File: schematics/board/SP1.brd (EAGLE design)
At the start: 30 x 38 mm, 12 parts

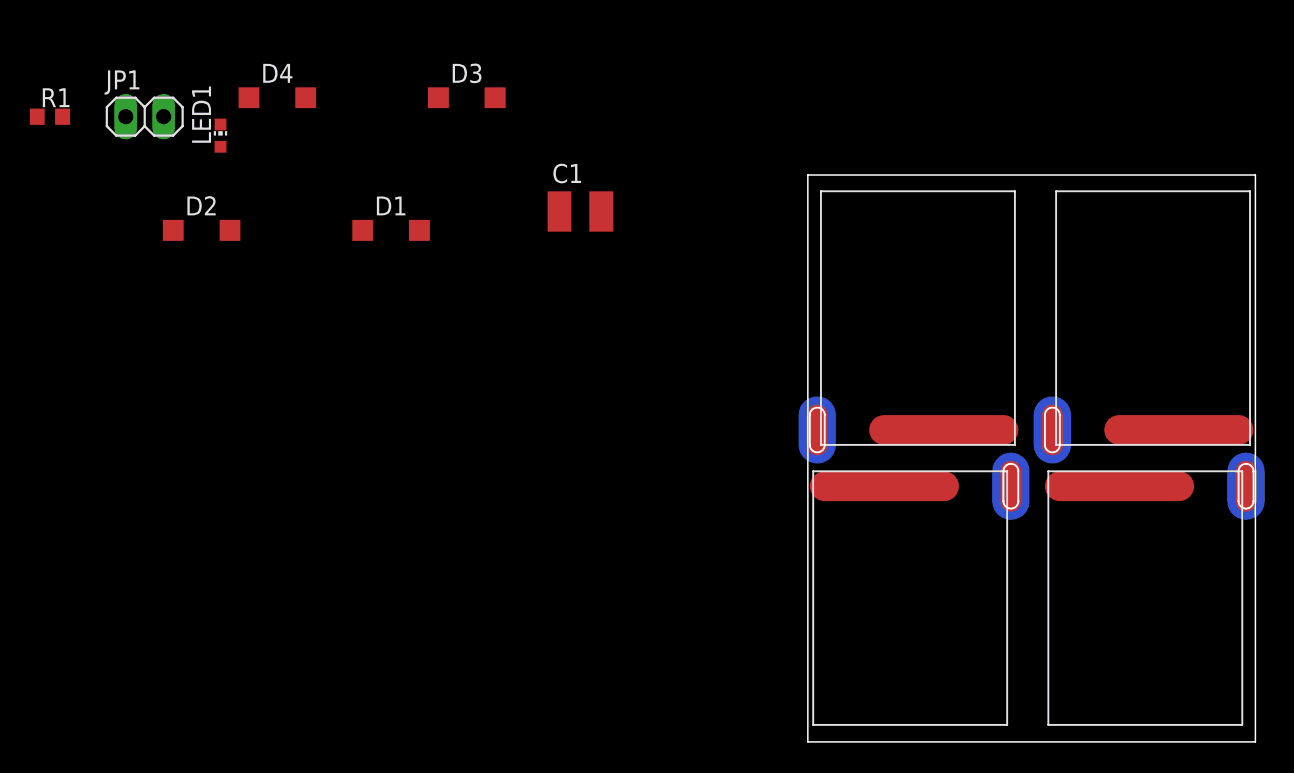
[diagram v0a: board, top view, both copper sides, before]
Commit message: развёл плату солнечных панелей(на деньги)
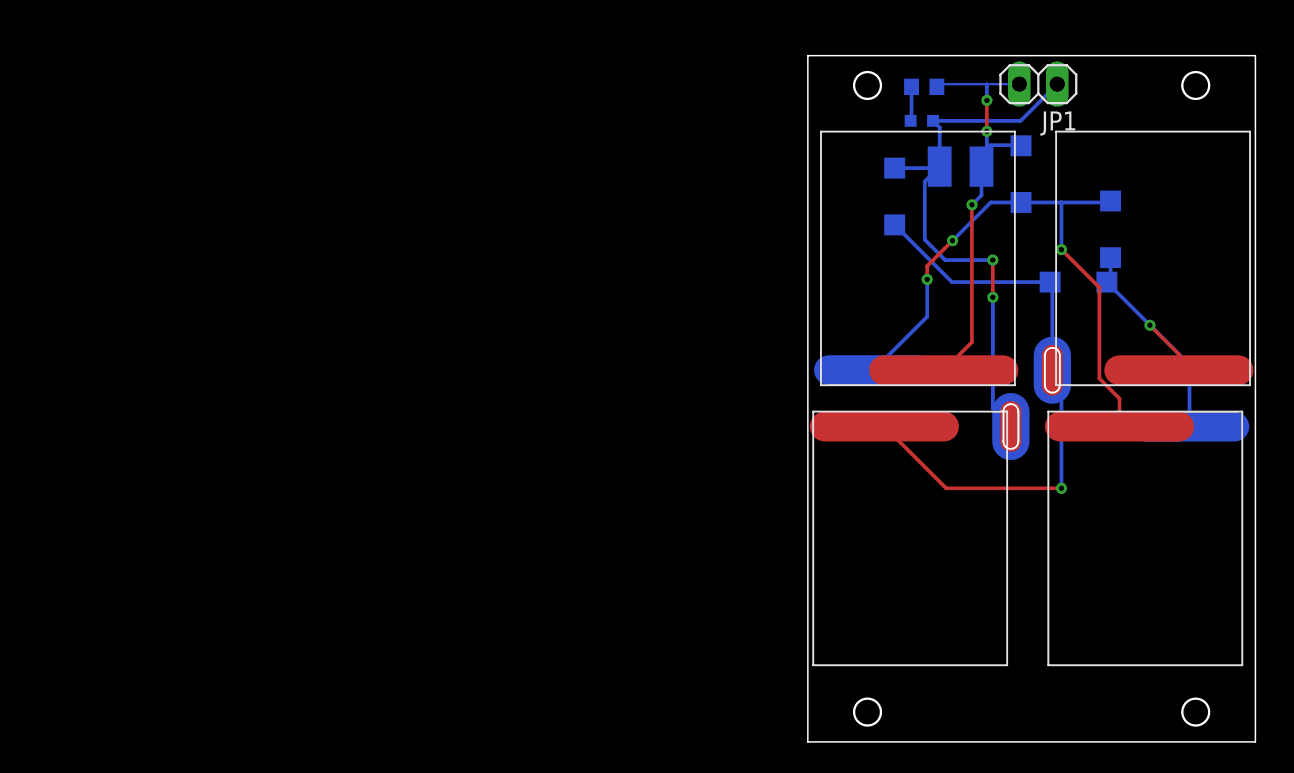
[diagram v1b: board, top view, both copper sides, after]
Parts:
- U$1, U$2: value SOLAR-2_0 -> SOLAR-2_1; device CanCubeSat:SOLAR_0-2 -> CanCubeSat:SOLAR_1-2
- moved D2 60.9 mm to (20.3, 34.4), flipped to the bottom, turned to 90 degrees
- moved JP1 59.9 mm to (15.4, 44.1), turned to 180 degrees
- moved R1 58.6 mm to (7.80, 43.9), flipped to the bottom
- moved LED1 47.0 mm to (7.64, 41.6), flipped to the bottom, turned to 90 degrees
- moved D3 42.8 mm to (18.1, 30.8), flipped to the bottom, turned to 180 degrees
- moved D1 42.4 mm to (14.3, 38.1), flipped to the bottom, turned to 90 degrees
- moved D4 41.9 mm to (5.82, 36.6), flipped to the bottom, turned to 270 degrees
- moved C1 25.7 mm to (10.2, 38.6), flipped to the bottom
- moved U$2 4.00 mm to (22.6, 13.6)
- moved U$4 4.00 mm to (6.86, 13.6)
- moved U$1 4.00 mm to (7.38, 32.4)
- moved U$3 4.00 mm to (23.1, 32.4)
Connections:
- net N$1: now also U$1.OUT; no longer U$1.OUT-2, U$1.OUT-21
- net N$2: now also U$2.OUT; no longer U$2.OUT-2, U$2.OUT-21
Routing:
- net N$1: track 0.00 -> 39.2 mm, vias 0 -> 3
- net SP-: track 0.00 -> 36.4 mm, vias 0 -> 2
- net N$3: track 0.00 -> 35.8 mm, vias 0 -> 1
- net SP+: track 0.00 -> 28.3 mm, vias 0 -> 3
- net N$2: track 0.00 -> 17.6 mm, vias 0 -> 1
- net N$4: track 0.00 -> 2.30 mm
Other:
- board size 30 x 38 mm -> 30 x 46 mm

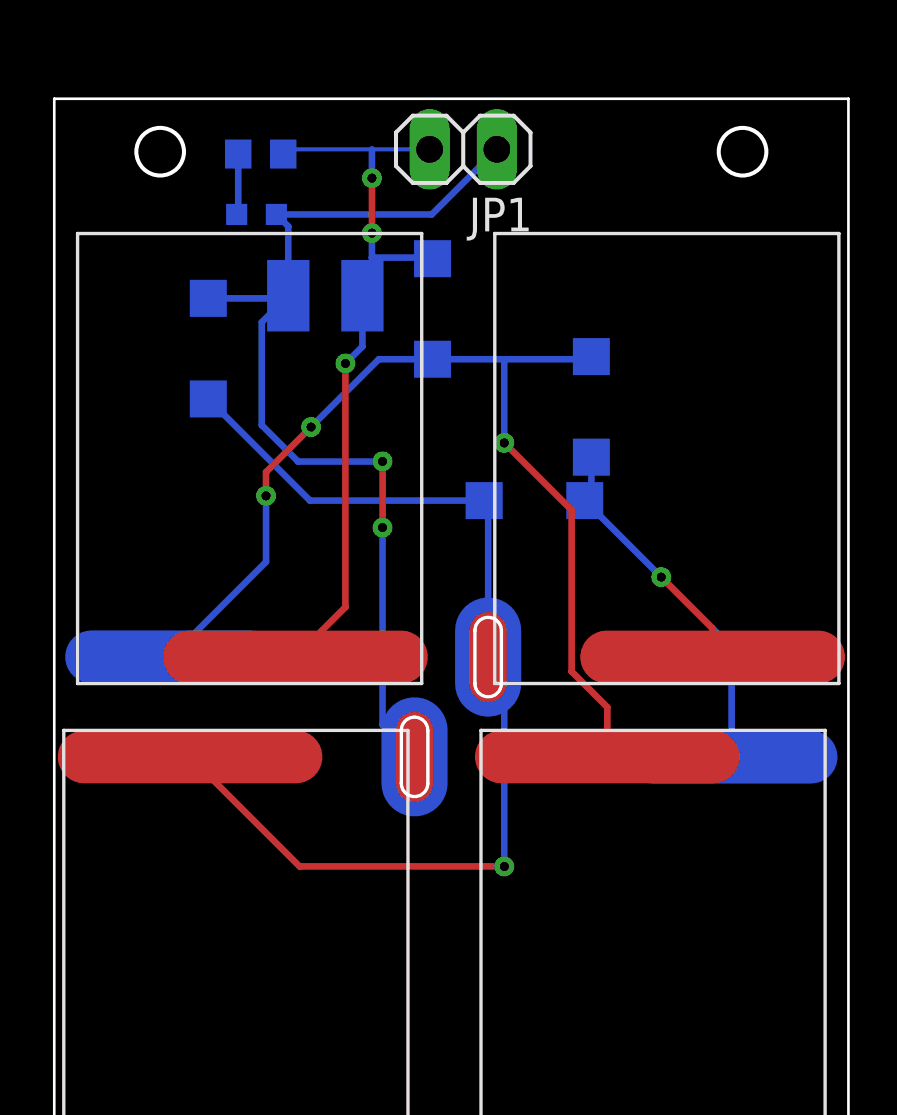
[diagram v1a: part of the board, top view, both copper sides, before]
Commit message: Добавлена плата мотора в сборку
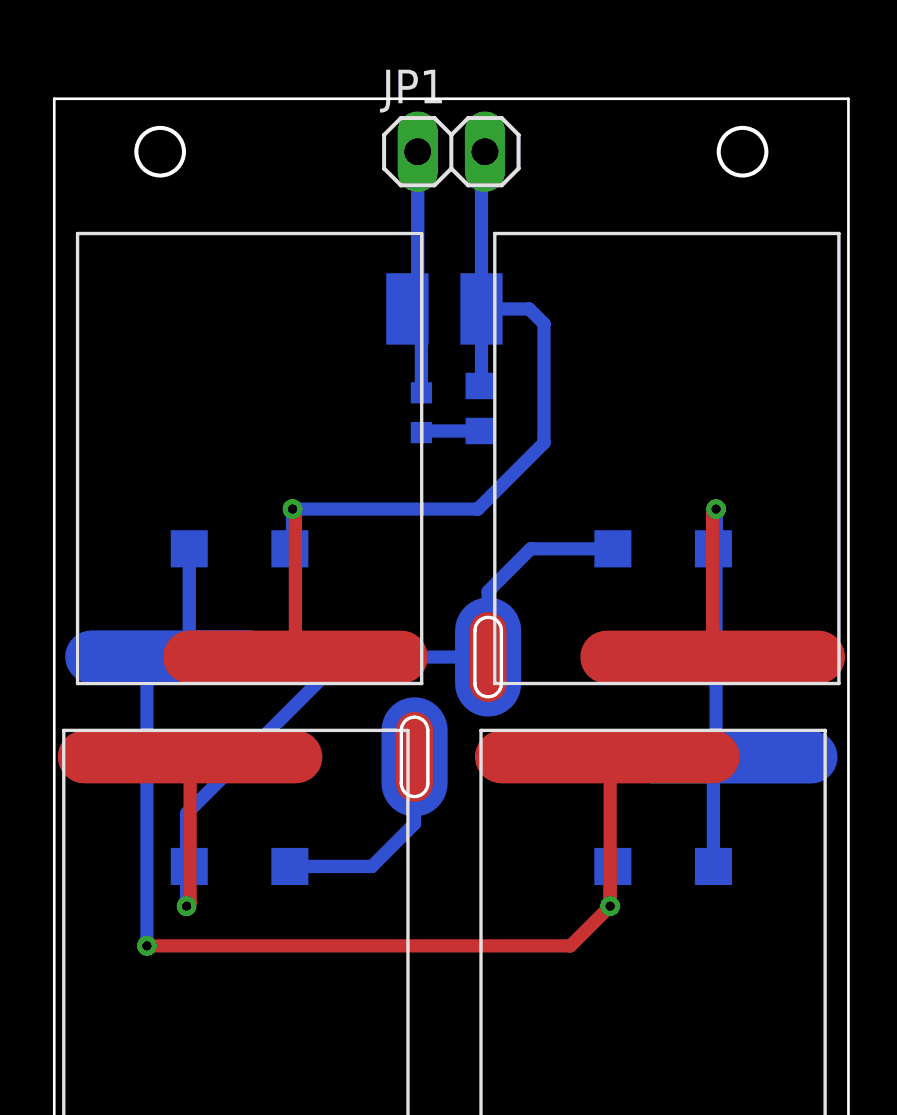
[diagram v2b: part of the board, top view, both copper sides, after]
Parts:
- moved D4 19.6 mm to (7.00, 17.0), turned to 0 degrees
- moved D2 17.6 mm to (23.0, 17.0), turned to 0 degrees
- moved R1 12.7 mm to (16.1, 34.3), turned to 270 degrees
- moved D1 11.6 mm to (7.00, 29.0), turned to 180 degrees
- moved LED1 9.74 mm to (13.9, 34.1), turned to 0 degrees
- moved D3 5.19 mm to (23.0, 29.0)
- moved C1 4.53 mm to (14.7, 38.1)
- moved JP1 0.46 mm to (15.0, 44.0), turned to 0 degrees
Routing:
- net SP-: track 36.4 -> 17.8 mm, vias 2 -> 0
- net SP+: track 28.3 -> 33.7 mm, vias 3 -> 1
- net N$3: track 35.8 -> 31.0 mm
- net N$2: track 17.6 -> 21.2 mm
- net N$1: track 39.2 -> 41.0 mm, vias 3 -> 2
